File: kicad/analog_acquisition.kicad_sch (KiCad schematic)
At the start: 47 parts, among them J1 BNC_Isolated, J2 BNC_Isolated, J3 JST-XH 3-pin, J4 BNC_Isolated, J5 JST-XH 2-pin, J6 JST-XH 3-pin, U3 MCP6002, U3_2 MCP6002

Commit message: fix: Embed lib_symbols, fix invalid lib_ids, bump to KiCad 9 format
- Embed complete (lib_symbols) definitions in all 5 sub-sheets so symbols
  render as real parts instead of '??' placeholders (files now self-contained)
- Substitute invalid lib_ids with valid library symbols:
  Device:CP -> Device:C_Polarized, Diode:PESD3V3S2USF -> Diode:PESD3V3S1UL,
  Diode:PESD5V0S1BSF -> Diode:PESD5V0S1UL, Isolator:PC817X2 -> Isolator:PC817
- Bump file format version 20231120 -> 20250114 (removes 'older version' warning)
- Left-justify header text blocks so long lines stay within the A3 frame

Validated: kicad-cli SVG render (all real symbols, within frame), clean-room
eeschema GUI render with broken library table (no '??'), and kicad-cli ERC
runs without crashing (425 violations are expected unconnected-pin/dangling-
label items, resolved during per-sheet wiring).

Co-Authored-By: Devin AI <158243242+devin-ai-integration[bot]@users.noreply.github.com>
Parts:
- D3, D4, D5, D6, D6_CO2, D_DO: symbol Diode:PESD5V0S1BSF -> Diode:PESD5V0S1UL
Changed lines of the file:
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@@
 (kicad_sch
-  (version 20231120)
+  (version 20250114)
   (generator "devin")
   (generator_version "1.0")
@@
   )
   (symbol
-    (lib_id "Diode:PESD5V0S1BSF")
+    (lib_id "Diode:PESD5V0S1UL")
     (at 43.18 50.8 0)
     (unit 1)
@@
   )
   (symbol
-    (lib_id "Diode:PESD5V0S1BSF")
+    (lib_id "Diode:PESD5V0S1UL")
     (at 43.18 88.9 0)
     (unit 1)
@@
   )
   (symbol
-    (lib_id "Diode:PESD5V0S1BSF")
+    (lib_id "Diode:PESD5V0S1UL")
     (at 43.18 127.0 0)
     (unit 1)
@@
   )
   (symbol
-    (lib_id "Diode:PESD5V0S1BSF")
+    (lib_id "Diode:PESD5V0S1UL")
     (at 43.18 165.1 0)
     (unit 1)
@@
   )
   (symbol
-    (lib_id "Diode:PESD5V0S1BSF")
+    (lib_id "Diode:PESD5V0S1UL")
     (at 43.18 203.2 0)
     (unit 1)
@@
   )
   (symbol
-    (lib_id "Diode:PESD5V0S1BSF")
+    (lib_id "Diode:PESD5V0S1UL")
     (at 43.18 241.3 0)
     (unit 1)
@@
   (text "ANALOG ACQUISITION — 6 channels with on-board galvanic isolation\nEach wet sensor (pH, ORP, DO) has dedicated SN6501+ADuM1250 isolation barrier\nAll channels: Connector → TVS ESD → RC filter → Op-amp buffer → ADC\nPull-downs 10M prevent floating reads when sensor disconnected"
     (at 25.4 15.24 0)
-    (effects (font (size 2.54 2.54)))
+    (effects (font (size 2.54 2.54)) (justify left))
   )
 )

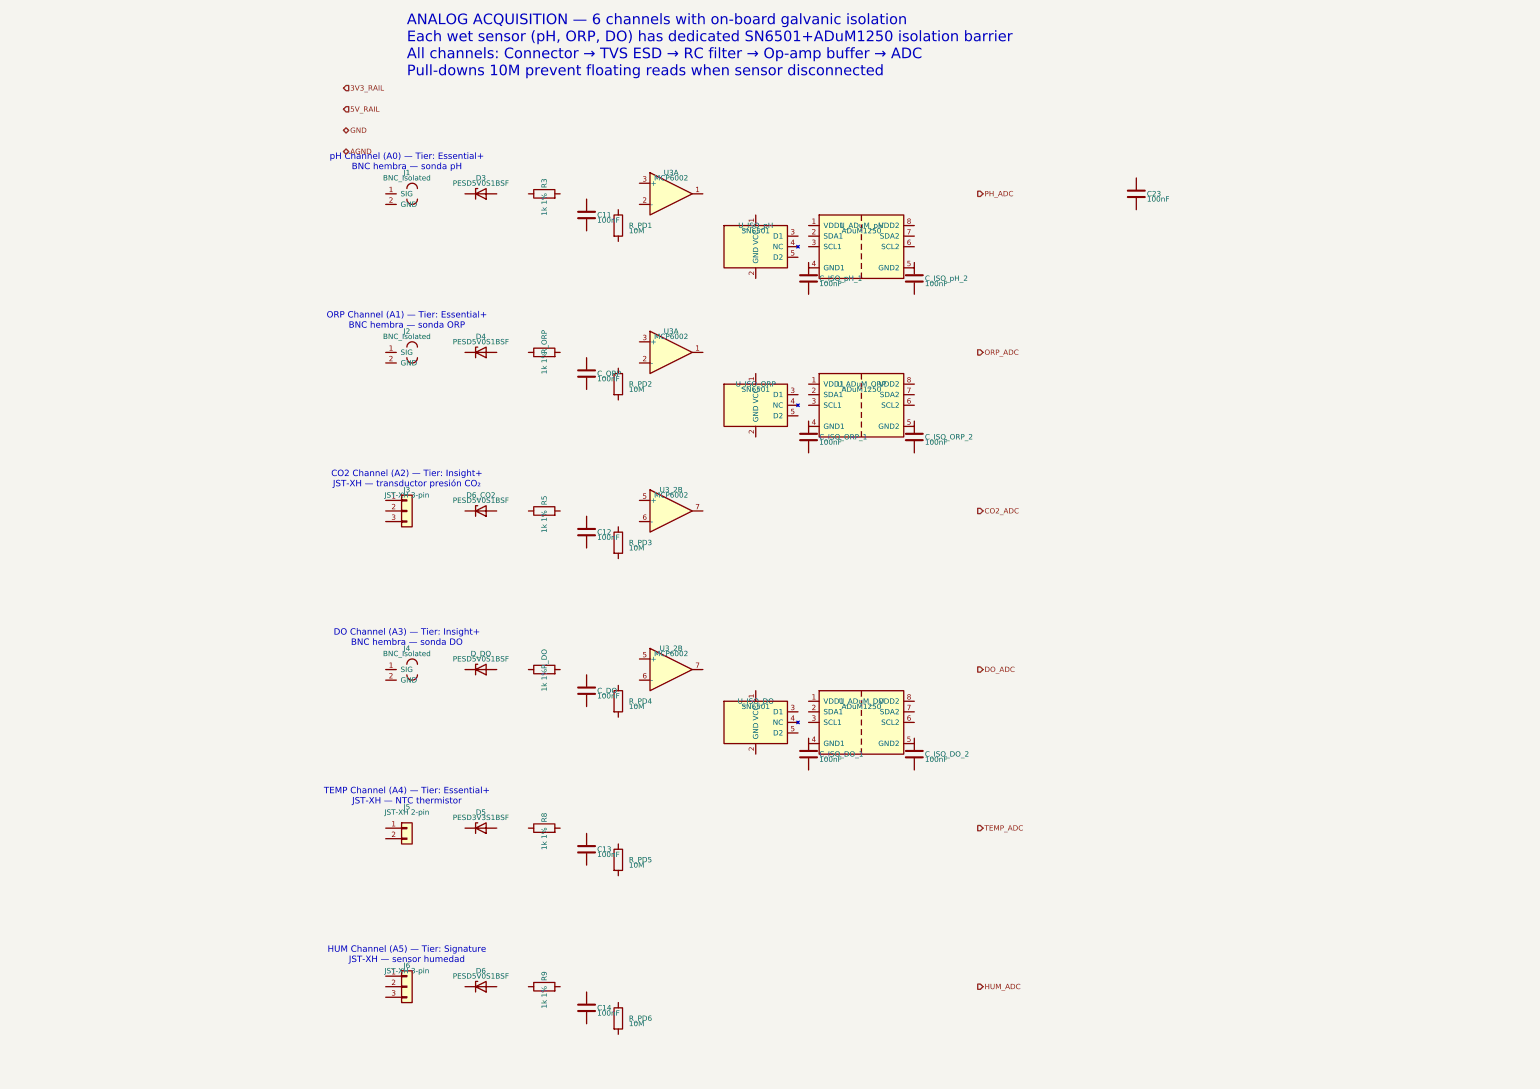
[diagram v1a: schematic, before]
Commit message: fix: Re-annotate components with unique global references + add instances blocks
Root cause: symbol instances lacked (instances ...) blocks, so KiCad treated
all references as unannotated/duplicated (108 duplicate_reference ERC errors)
and produced auto-renamed names (C_DO2, U3_2A, ...) on annotation.

Fix: assign globally-unique sequential standard references (R1..R28, C1..C27,
U1..U20, D1..D18, J1..J21, etc.) and embed a proper (instances) block per
symbol with the correct hierarchical path. Each MCP6002 kept as its own IC
(unit A) to preserve per-channel galvanic isolation (pH/ORP/DO).

ERC: duplicate_reference 108 -> 0, unannotated 1 -> 0.
Co-Authored-By: Devin AI <158243242+devin-ai-integration[bot]@users.noreply.github.com>
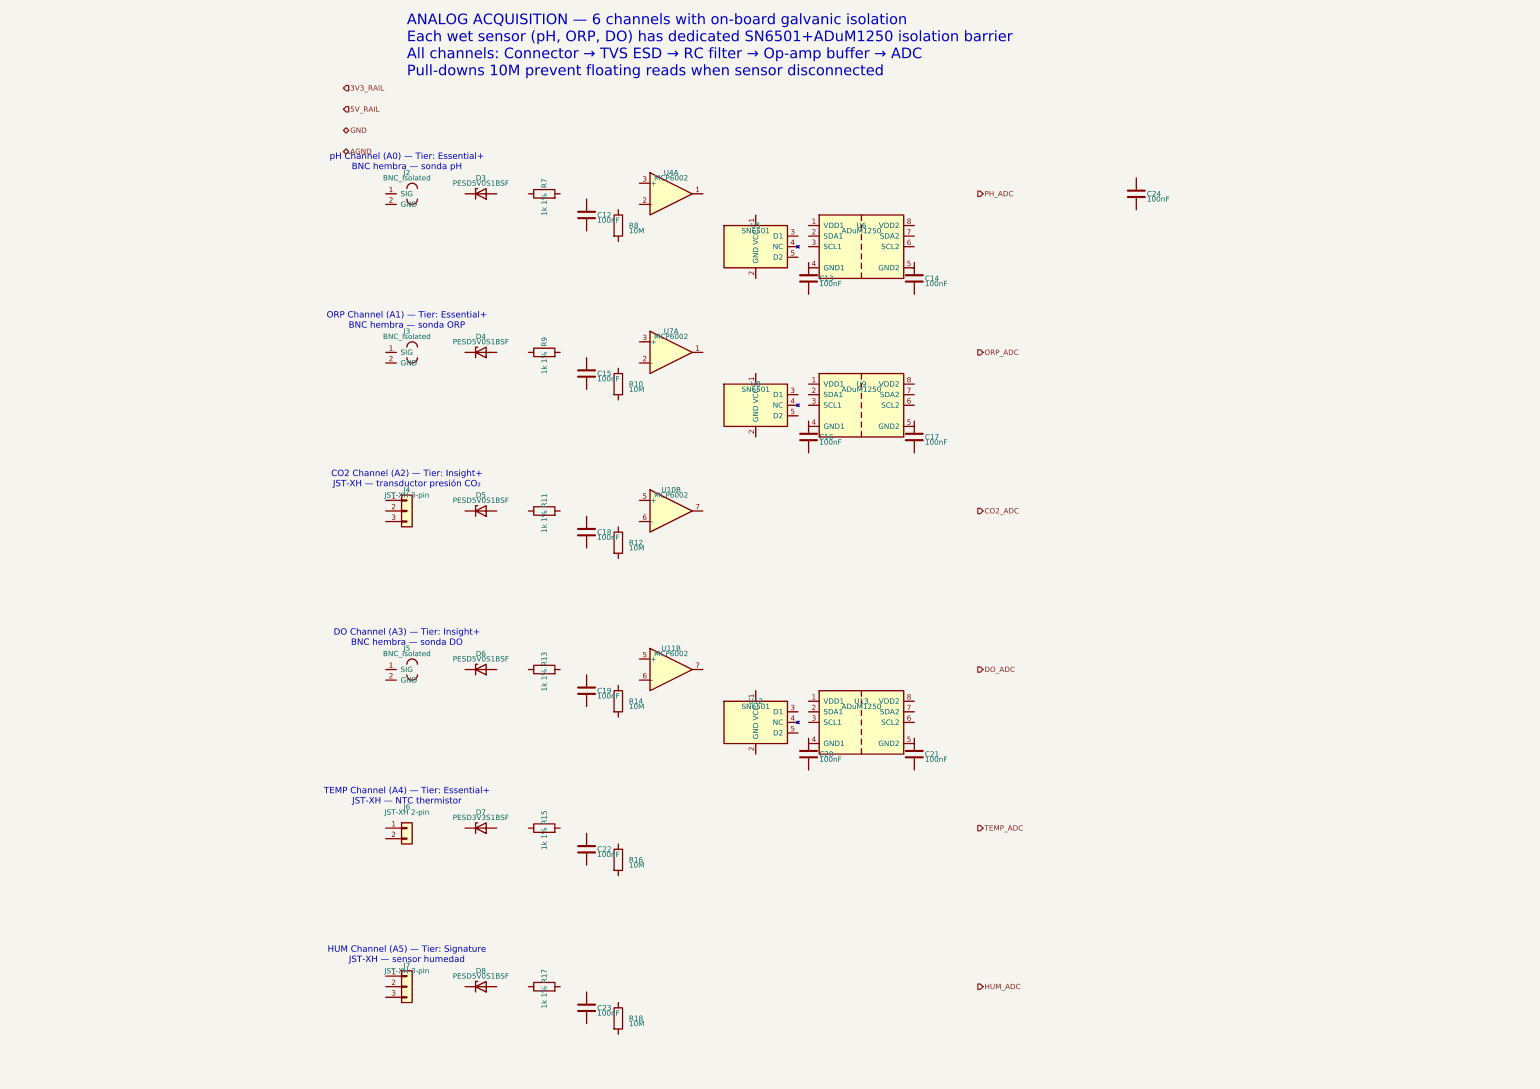
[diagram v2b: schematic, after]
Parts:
- renumbered C11 to C12, C_ISO_pH_1 to C13, C_ISO_pH_2 to C14, C_ORP to C15, C_ISO_ORP_1 to C16, C_ISO_ORP_2 to C17, C12 to C18, C_DO to C19, C_ISO_DO_1 to C20, C_ISO_DO_2 to C21, C13 to C22, C14 to C23, C23 to C24, D6_CO2 to D5, D_DO to D6, D5 to D7, D6 to D8, J1 to J2, J2 to J3, J3 to J4, J4 to J5, J5 to J6, J6 to J7, R_PD2 to R10, R5 to R11, R_PD3 to R12, R_DO to R13, R_PD4 to R14, R8 to R15, R_PD5 to R16, R9 to R17, R_PD6 to R18, R3 to R7, R_PD1 to R8, R_ORP to R9, U3_2 to U10, U3_2 to U11, U_ISO_DO to U12, U_ADuM_DO to U13, U3 to U4, U_ISO_pH to U5, U_ADuM_pH to U6, U3 to U7, U_ISO_ORP to U8, U_ADuM_ORP to U9

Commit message: feat: Wire analog_acquisition — B2 AMC1301 isolation + SN6501 isolated supplies
6-channel wiring with B2 architecture:

Isolated channels (pH/ORP/DO):
- Electrode → ESD → R series → RC filter → MCP6002 buffer →
  AMC1301 (analog isolation) → *_ADC hierarchical label
- SN6501-driven transformer (SP_2S) + Schottky rectifier +
  10µF reservoir cap for real isolated DC supply (VDD_ISO_x)
- Each channel has independent op-amp + AMC + isolated supply
- Op-amp units B (follower to GND) and C (power) placed per chip

Non-isolated channels (CO2/Temp/Hum):
- Connector → ESD → R series → RC filter → (op-amp buffer where
  applicable) → *_ADC hierarchical label
- Unit-aware op-amp wiring via get_unit() (U10=unit2, U11=unit2)

Power rails:
- PWR_FLAGs on 5V_RAIL and 3V3_RAIL drive power inputs
- C24 wired as 3V3 decoupling cap
- GND distribution via power:GND symbols

ERC validation (kicad-cli):
- Analog Acquisition sheet: 0 violations
- trace_net: 0 shorts (no net collisions)
- 310 total project violations (all in unwired sheets)

Co-Authored-By: Devin AI <158243242+devin-ai-integration[bot]@users.noreply.github.com>
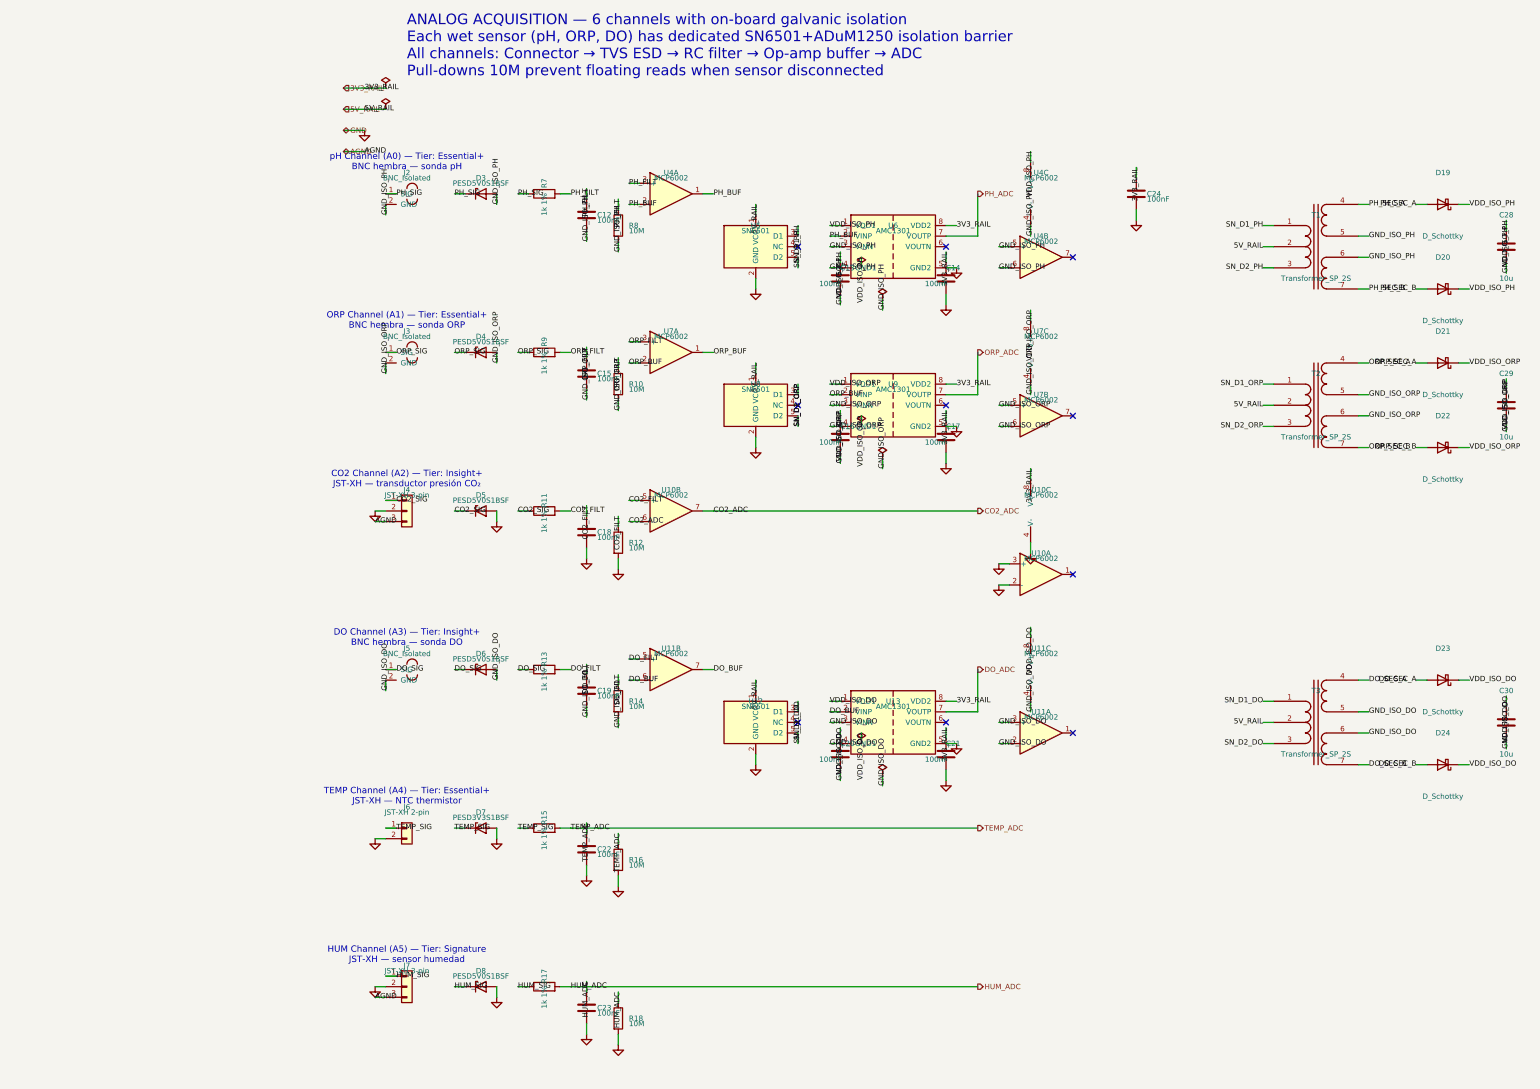
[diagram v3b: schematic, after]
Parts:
- added C28, C29, C30: 10u, Capacitor_SMD:C_0805_2012Metric, symbol Device:C
- added D19, D20, D21, D22, D23, D24: D_Schottky, Diode_SMD:D_SOD-123, symbol Device:D_Schottky
- added T1, T2, T3: Transformer_SP_2S, symbol Device:Transformer_SP_2S
- added unit 1 of U10
- added unit 3 of U10
- added unit 1 of U11
- added unit 3 of U11
- added unit 3 of U4
- added unit 2 of U4
- added unit 2 of U7
- added unit 3 of U7
- U13, U6, U9: value ADuM1250 -> AMC1301; symbol nebula_symbols:ADuM1250ARZ -> nebula_symbols:AMC1301DWVR; MPN ADuM1250ARZ -> AMC1301DWVR
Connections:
- net 3V3_RAIL: now also C14.1, C17.1, C21.1, C24.1, U13.8 (VDD2), U6.8 (VDD2), U9.8 (VDD2), U10.8 (V+)
- net 5V_RAIL: now also U12.1 (VCC), U5.1 (VCC), U8.1 (VCC), T1.2 (PM), T2.2 (PM), T3.2 (PM)
- net AGND: now also J4.3 (Pin_3), J7.3 (Pin_3)
- net CO2_ADC: now also U10.6 (-), U10.7
- net DO_ADC: now also U13.7 (VOUTP)
- net GND: now also C14.2, C17.2, C18.2, C21.2, C22.2, C23.2, C24.2, D5.2 (A), D7.2 (A), D8.2 (A), J4.2 (Pin_2), J6.2 (Pin_2), J7.2 (Pin_2), R12.2, R16.2, R18.2, U12.2 (GND), U13.5 (GND2), U5.2 (GND), U6.5 (GND2), U8.2 (GND), U9.5 (GND2), U10.2 (-), U10.3 (+), U10.4 (V-)
- net HUM_ADC: now also C23.1, R17.2, R18.1
- net ORP_ADC: now also U9.7 (VOUTP)
- net PH_ADC: now also U6.7 (VOUTP)
- net TEMP_ADC: now also C22.1, R15.2, R16.1
- net VDD_ISO_PH: now reaches U6.1 (VDD1)
- net VDD_ISO_PH: now also C13.1, C28.1, D19.1 (K), D20.1 (K), U4.8 (V+)
- net PH_BUF: now reaches U6.2 (VINP)
- net PH_BUF: now also U4.1, U4.2 (-)
- net GND_ISO_PH: now reaches U6.3 (VINN)
- net GND_ISO_PH: now also C12.2, C13.2, D3.2 (A), J2.2 (GND), R8.2, U6.4 (GND1), C28.2, T1.5 (OUT1B), T1.6 (OUT2A), U4.4 (V-), U4.5 (+), U4.6 (-)
- net CO2_FILT: now reaches C18.1
- net CO2_FILT: now also R11.2, R12.1, U10.5 (+)
- net ORP_BUF: now reaches U7.1
- net ORP_BUF: now also U7.2 (-), U9.2 (VINP)
- net ORP_FILT: now reaches U7.3 (+)
- net ORP_FILT: now also C15.1, R10.1, R9.2
- net DO_SIG: now reaches D6.1 (K)
- net DO_SIG: now also J5.1 (SIG), R13.1
- net GND_ISO_DO: now reaches D6.2 (A)
- net GND_ISO_DO: now also C19.2, C20.2, J5.2 (GND), R14.2, U13.3 (VINN), U13.4 (GND1), C30.2, T3.5 (OUT1B), T3.6 (OUT2A), U11.2 (-), U11.3 (+), U11.4 (V-)
- net DO_FILT: now reaches C19.1
- net DO_FILT: now also R13.2, R14.1, U11.5 (+)
- net HUM_SIG: now reaches R17.1
- net HUM_SIG: now also D8.1 (K), J7.1 (Pin_1)
- net GND_ISO_ORP: now reaches C15.2
- net GND_ISO_ORP: now also C16.2, D4.2 (A), J3.2 (GND), R10.2, U9.3 (VINN), U9.4 (GND1), C29.2, T2.5 (OUT1B), T2.6 (OUT2A), U7.4 (V-), U7.5 (+), U7.6 (-)
- net TEMP_SIG: now reaches R15.1
- net TEMP_SIG: now also D7.1 (K), J6.1 (Pin_1)
- net SN_D1_ORP: now reaches U8.3 (D1)
- net SN_D1_ORP: now also T2.1 (IN+)
- net SN_D2_ORP: now reaches U8.5 (D2)
- net SN_D2_ORP: now also T2.3 (IN-)
- net PH_FILT: now reaches R8.1
- net PH_FILT: now also C12.1, R7.2, U4.3 (+)
- net VDD_ISO_DO: now reaches U13.1 (VDD1)
- net VDD_ISO_DO: now also C20.1, C30.1, D23.1 (K), D24.1 (K), U11.8 (V+)
- net DO_BUF: now reaches U13.2 (VINP)
- net DO_BUF: now also U11.6 (-), U11.7
- net ORP_SIG: now reaches J3.1 (SIG)
- net ORP_SIG: now also D4.1 (K), R9.1
- net VDD_ISO_ORP: now reaches C16.1
- net VDD_ISO_ORP: now also U9.1 (VDD1), C29.1, D21.1 (K), D22.1 (K), U7.8 (V+)
- net SN_D1_DO: now reaches U12.3 (D1)
- net SN_D1_DO: now also T3.1 (IN+)
- net SN_D2_DO: now reaches U12.5 (D2)
- net SN_D2_DO: now also T3.3 (IN-)
- net CO2_SIG: now reaches R11.1
- net CO2_SIG: now also D5.1 (K), J4.1 (Pin_1)
- net PH_SIG: now reaches J2.1 (SIG)
- net PH_SIG: now also D3.1 (K), R7.1
- net SN_D1_PH: now reaches U5.3 (D1)
- net SN_D1_PH: now also T1.1 (IN+)
- net SN_D2_PH: now reaches U5.5 (D2)
- net SN_D2_PH: now also T1.3 (IN-)
- new net DO_SEC_A: D23.2 (A), T3.4 (OUT1A)
- new net DO_SEC_B: D24.2 (A), T3.7 (OUT2B)
- new net ORP_SEC_A: D21.2 (A), T2.4 (OUT1A)
- new net ORP_SEC_B: D22.2 (A), T2.7 (OUT2B)
- new net PH_SEC_A: D19.2 (A), T1.4 (OUT1A)
- new net PH_SEC_B: D20.2 (A), T1.7 (OUT2B)
- no-connect marks 0 -> 10
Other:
- moved on the sheet: C13, C14, C16, C17, C20, C21, U13, U6, U9
